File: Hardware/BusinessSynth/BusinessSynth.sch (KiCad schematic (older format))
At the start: 63 parts, among them J1 StylusKey, J2 StylusKey, J3 StylusKey, J4 StylusKey, J5 StylusKey, J6 StylusKey, J7 StylusKey, J8 StylusKey, J9 StylusKey, Q1 Q_PNP_BEC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

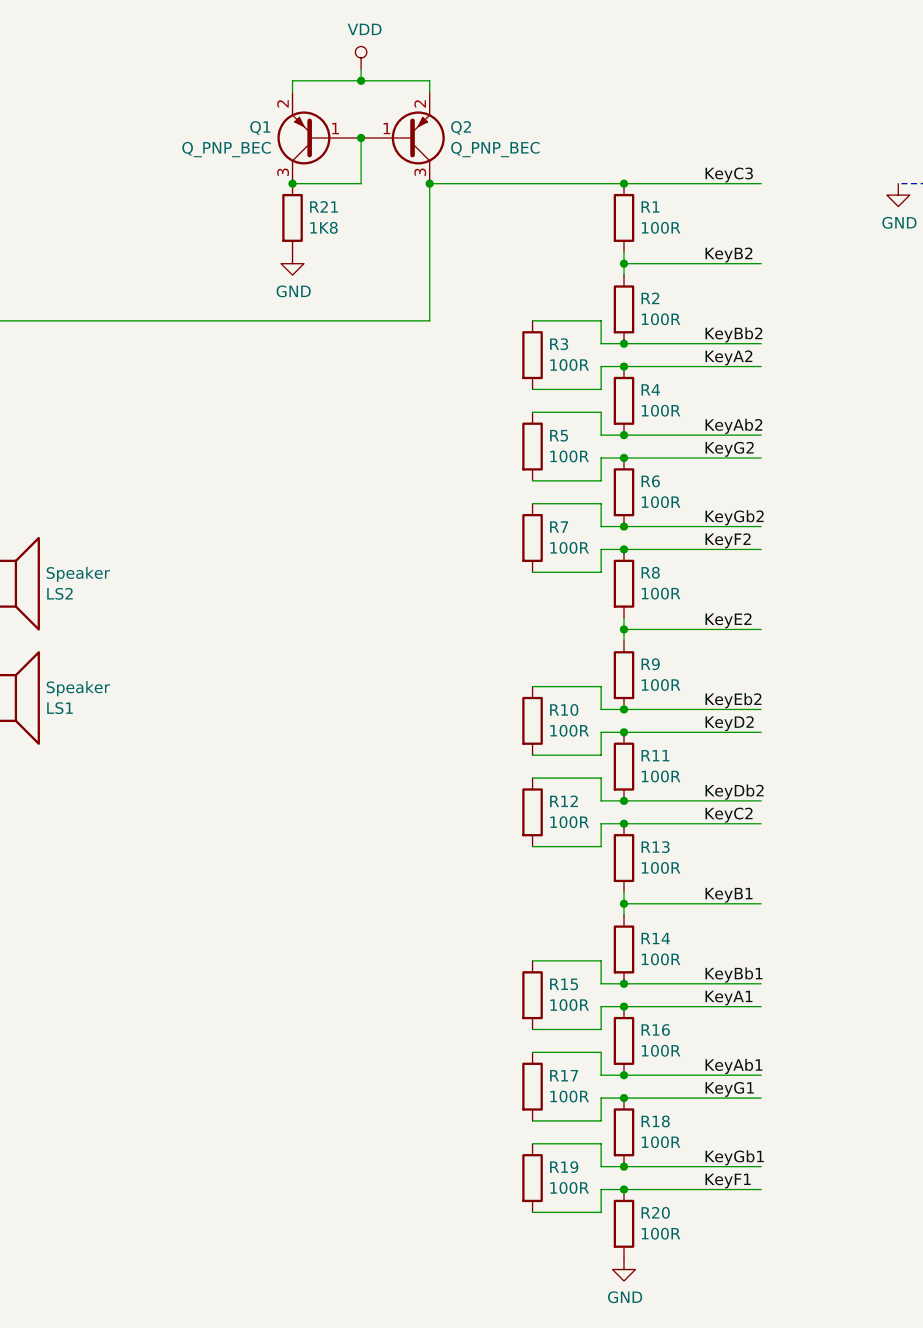
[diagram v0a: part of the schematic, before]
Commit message: Draw new keyboard circuit in the KiCAD schematic
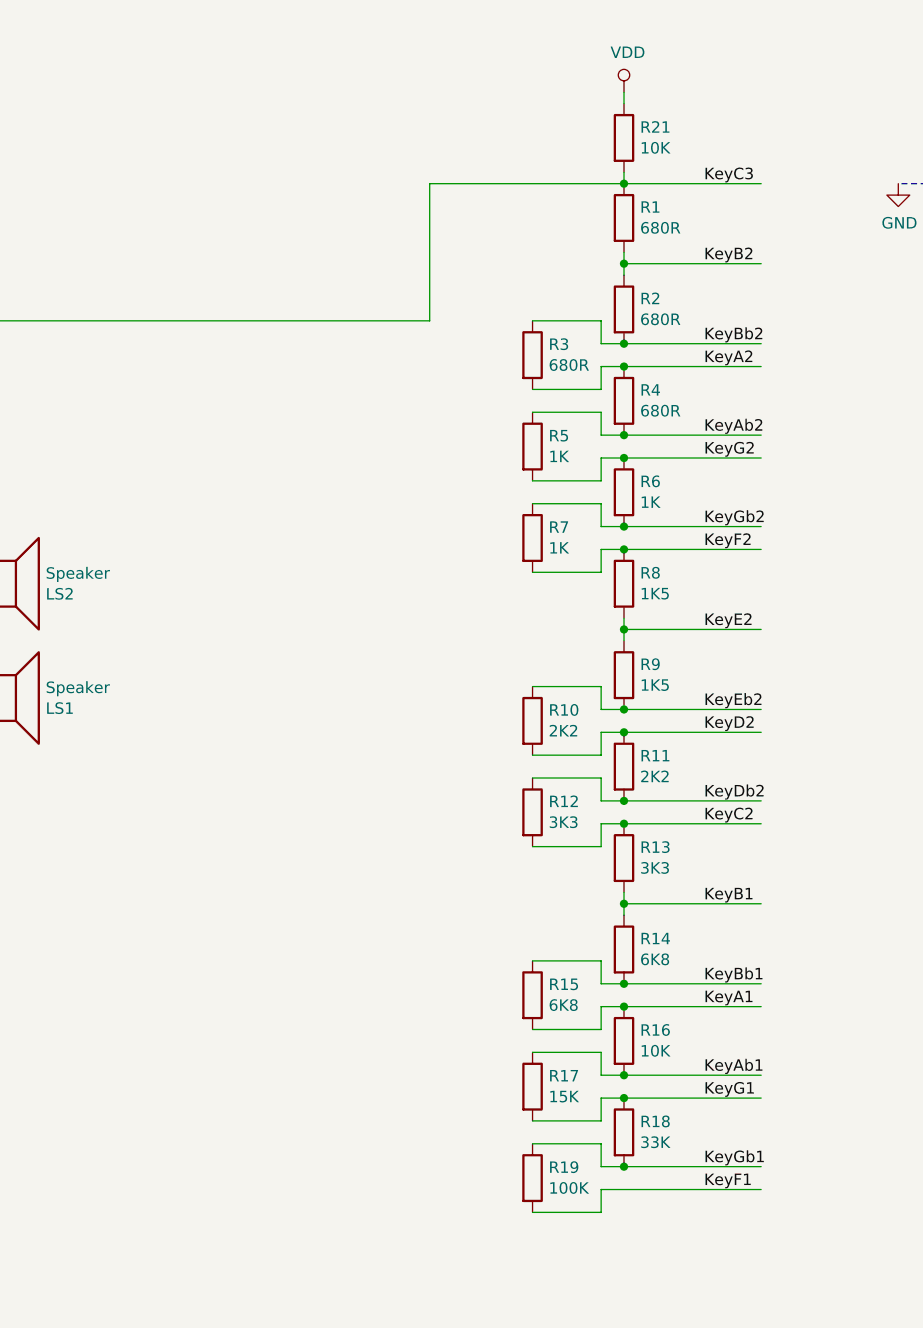
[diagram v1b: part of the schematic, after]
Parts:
- removed Q1, Q2: Q_PNP_BEC, BusinessSynth:SOT-323_SC-70_nosilk, symbol Device:Q_PNP_BEC
- removed R20: 100R, BusinessSynth:R_0603_1608Metric_nosilk, symbol Device:R
- R1, R2, R3, R4: value 100R -> 680R
- R10, R11: value 100R -> 2K2
- R12, R13: value 100R -> 3K3
- R14, R15: value 100R -> 6K8
- R16: value 100R -> 10K
- R17: value 100R -> 15K
- R18: value 100R -> 33K
- R19: value 100R -> 100K
- R21: value 1K8 -> 10K
- R5, R6, R7: value 100R -> 1K
- R8, R9: value 100R -> 1K5
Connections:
- wire segments 177 -> 171
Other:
- moved on the sheet: R21
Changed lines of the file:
@@
 P 9350 1450
 F 0 "R1" H 9420 1496 50  0000 L CNN
-F 1 "100R" H 9420 1405 50  0000 L CNN
+F 1 "680R" H 9420 1405 50  0000 L CNN
 F 2 "BusinessSynth:R_0603_1608Metric_nosilk" V 9280 1450 50  0001 C CNN
 F 3 "~" H 9350 1450 50  0001 C CNN
@@
 P 9350 1850
 F 0 "R2" H 9420 1896 50  0000 L CNN
-F 1 "100R" H 9420 1805 50  0000 L CNN
+F 1 "680R" H 9420 1805 50  0000 L CNN
 F 2 "BusinessSynth:R_0603_1608Metric_nosilk" V 9280 1850 50  0001 C CNN
 F 3 "~" H 9350 1850 50  0001 C CNN
@@
 P 9350 2250
 F 0 "R4" H 9420 2296 50  0000 L CNN
-F 1 "100R" H 9420 2205 50  0000 L CNN
+F 1 "680R" H 9420 2205 50  0000 L CNN
 F 2 "BusinessSynth:R_0603_1608Metric_nosilk" V 9280 2250 50  0001 C CNN
 F 3 "~" H 9350 2250 50  0001 C CNN
@@
 P 9350 2650
 F 0 "R6" H 9420 2696 50  0000 L CNN
-F 1 "100R" H 9420 2605 50  0000 L CNN
+F 1 "1K" H 9420 2605 50  0000 L CNN
 F 2 "BusinessSynth:R_0603_1608Metric_nosilk" V 9280 2650 50  0001 C CNN
 F 3 "~" H 9350 2650 50  0001 C CNN
@@
 P 9350 3050
 F 0 "R8" H 9420 3096 50  0000 L CNN
-F 1 "100R" H 9420 3005 50  0000 L CNN
+F 1 "1K5" H 9420 3005 50  0000 L CNN
 F 2 "BusinessSynth:R_0603_1608Metric_nosilk" V 9280 3050 50  0001 C CNN
 F 3 "~" H 9350 3050 50  0001 C CNN
@@
 P 9350 3450
 F 0 "R9" H 9420 3496 50  0000 L CNN
-F 1 "100R" H 9420 3405 50  0000 L CNN
+F 1 "1K5" H 9420 3405 50  0000 L CNN
 F 2 "BusinessSynth:R_0603_1608Metric_nosilk" V 9280 3450 50  0001 C CNN
 F 3 "~" H 9350 3450 50  0001 C CNN
@@
 P 9350 3850
 F 0 "R11" H 9420 3896 50  0000 L CNN
-F 1 "100R" H 9420 3805 50  0000 L CNN
+F 1 "2K2" H 9420 3805 50  0000 L CNN
 F 2 "BusinessSynth:R_0603_1608Metric_nosilk" V 9280 3850 50  0001 C CNN
 F 3 "~" H 9350 3850 50  0001 C CNN
@@
 P 9350 4250
 F 0 "R13" H 9420 4296 50  0000 L CNN
-F 1 "100R" H 9420 4205 50  0000 L CNN
+F 1 "3K3" H 9420 4205 50  0000 L CNN
 F 2 "BusinessSynth:R_0603_1608Metric_nosilk" V 9280 4250 50  0001 C CNN
 F 3 "~" H 9350 4250 50  0001 C CNN
@@
 P 9350 4650
 F 0 "R14" H 9420 4696 50  0000 L CNN
-F 1 "100R" H 9420 4605 50  0000 L CNN
+F 1 "6K8" H 9420 4605 50  0000 L CNN
 F 2 "BusinessSynth:R_0603_1608Metric_nosilk" V 9280 4650 50  0001 C CNN
 F 3 "~" H 9350 4650 50  0001 C CNN
@@
 P 9350 5050
 F 0 "R16" H 9420 5096 50  0000 L CNN
-F 1 "100R" H 9420 5005 50  0000 L CNN
+F 1 "10K" H 9420 5005 50  0000 L CNN
 F 2 "BusinessSynth:R_0603_1608Metric_nosilk" V 9280 5050 50  0001 C CNN
 F 3 "~" H 9350 5050 50  0001 C CNN
@@
 P 9350 5450
 F 0 "R18" H 9420 5496 50  0000 L CNN
-F 1 "100R" H 9420 5405 50  0000 L CNN
+F 1 "33K" H 9420 5405 50  0000 L CNN
 F 2 "BusinessSynth:R_0603_1608Metric_nosilk" V 9280 5450 50  0001 C CNN
 F 3 "~" H 9350 5450 50  0001 C CNN
 	1    9350 5450
-	1    0    0    -1
-$EndComp
-$Comp
-L Device:R R20
-U 1 1 5CA2AC61
-P 9350 5850
-F 0 "R20" H 9420 5896 50  0000 L CNN
-F 1 "100R" H 9420 5805 50  0000 L CNN
-F 2 "BusinessSynth:R_0603_1608Metric_nosilk" V 9280 5850 50  0001 C CNN
-F 3 "~" H 9350 5850 50  0001 C CNN
-	1    9350 5850
 	1    0    0    -1
 $EndComp
@@
 P 8950 2050
 F 0 "R3" H 9020 2096 50  0000 L CNN
-F 1 "100R" H 9020 2005 50  0000 L CNN
+F 1 "680R" H 9020 2005 50  0000 L CNN
 F 2 "BusinessSynth:R_0603_1608Metric_nosilk" V 8880 2050 50  0001 C CNN
 F 3 "~" H 8950 2050 50  0001 C CNN
@@
 P 8950 2450
 F 0 "R5" H 9020 2496 50  0000 L CNN
-F 1 "100R" H 9020 2405 50  0000 L CNN
+F 1 "1K" H 9020 2405 50  0000 L CNN
 F 2 "BusinessSynth:R_0603_1608Metric_nosilk" V 8880 2450 50  0001 C CNN
 F 3 "~" H 8950 2450 50  0001 C CNN
@@
 P 8950 2850
 F 0 "R7" H 9020 2896 50  0000 L CNN
-F 1 "100R" H 9020 2805 50  0000 L CNN
+F 1 "1K" H 9020 2805 50  0000 L CNN
 F 2 "BusinessSynth:R_0603_1608Metric_nosilk" V 8880 2850 50  0001 C CNN
 F 3 "~" H 8950 2850 50  0001 C CNN
@@
 P 8950 3650
 F 0 "R10" H 9020 3696 50  0000 L CNN
-F 1 "100R" H 9020 3605 50  0000 L CNN
+F 1 "2K2" H 9020 3605 50  0000 L CNN
 F 2 "BusinessSynth:R_0603_1608Metric_nosilk" V 8880 3650 50  0001 C CNN
 F 3 "~" H 8950 3650 50  0001 C CNN
@@
 P 8950 4050
 F 0 "R12" H 9020 4096 50  0000 L CNN
-F 1 "100R" H 9020 4005 50  0000 L CNN
+F 1 "3K3" H 9020 4005 50  0000 L CNN
 F 2 "BusinessSynth:R_0603_1608Metric_nosilk" V 8880 4050 50  0001 C CNN
 F 3 "~" H 8950 4050 50  0001 C CNN
@@
 P 8950 4850
 F 0 "R15" H 9020 4896 50  0000 L CNN
-F 1 "100R" H 9020 4805 50  0000 L CNN
+F 1 "6K8" H 9020 4805 50  0000 L CNN
 F 2 "BusinessSynth:R_0603_1608Metric_nosilk" V 8880 4850 50  0001 C CNN
 F 3 "~" H 8950 4850 50  0001 C CNN
@@
 P 8950 5250
 F 0 "R17" H 9020 5296 50  0000 L CNN
-F 1 "100R" H 9020 5205 50  0000 L CNN
+F 1 "15K" H 9020 5205 50  0000 L CNN
 F 2 "BusinessSynth:R_0603_1608Metric_nosilk" V 8880 5250 50  0001 C CNN
 F 3 "~" H 8950 5250 50  0001 C CNN
@@
 P 8950 5650
 F 0 "R19" H 9020 5696 50  0000 L CNN
-F 1 "100R" H 9020 5605 50  0000 L CNN
+F 1 "100K" H 9020 5605 50  0000 L CNN
 F 2 "BusinessSynth:R_0603_1608Metric_nosilk" V 8880 5650 50  0001 C CNN
 F 3 "~" H 8950 5650 50  0001 C CNN
@@
 	9250 5800 9250 5700
 Wire Wire Line
-	9250 5700 9350 5700
-Wire Wire Line
-	9350 5700 9950 5700
-Connection ~ 9350 5700
-Wire Wire Line
 	9350 5600 9950 5600
 Connection ~ 9350 5600
@@
 Wire Wire Line
 	9350 1300 9950 1300
-$Comp
-L power:GND #PWR06
-U 1 1 5CA52483
-P 9350 6000
-F 0 "#PWR06" H 9350 5750 50  0001 C CNN
-F 1 "GND" H 9355 5827 50  0000 C CNN
-F 2 "" H 9350 6000 50  0001 C CNN
-F 3 "" H 9350 6000 50  0001 C CNN
-	1    9350 6000
-	1    0    0    -1
-$EndComp
 Text Label 9700 1300 0    50   ~ 0
 KeyC3
@@
 L Device:R R21
 U 1 1 5CA2F499
-P 7900 1450
-F 0 "R21" H 7970 1496 50  0000 L CNN
-F 1 "1K8" H 7970 1405 50  0000 L CNN
-F 2 "Resistor_SMD:R_0402_1005Metric" V 7830 1450 50  0001 C CNN
-F 3 "~" H 7900 1450 50  0001 C CNN
-	1    7900 1450
-	1    0    0    -1
-$EndComp
-$Comp
-L power:GND #PWR0104
-U 1 1 5CA2FA03
-P 7900 1600
-F 0 "#PWR0104" H 7900 1350 50  0001 C CNN
-F 1 "GND" H 7905 1427 50  0000 C CNN
-F 2 "" H 7900 1600 50  0001 C CNN
-F 3 "" H 7900 1600 50  0001 C CNN
-	1    7900 1600
+P 9350 1100
+F 0 "R21" H 9420 1146 50  0000 L CNN
+F 1 "10K" H 9420 1055 50  0000 L CNN
+F 2 "Resistor_SMD:R_0402_1005Metric" V 9280 1100 50  0001 C CNN
+F 3 "~" H 9350 1100 50  0001 C CNN
+	1    9350 1100
 	1    0    0    -1
 $EndComp
@@
 L power:VDD #PWR0105
 U 1 1 5CA35224
-P 8200 800
-F 0 "#PWR0105" H 8200 650 50  0001 C CNN
-F 1 "VDD" H 8217 973 50  0000 C CNN
-F 2 "" H 8200 800 50  0001 C CNN
-F 3 "" H 8200 800 50  0001 C CNN
-	1    8200 800
-	1    0    0    -1
-$EndComp
-Wire Wire Line
-	7900 850  7900 900
-Wire Wire Line
-	7900 850  8200 850
-Wire Wire Line
-	8200 850  8200 800
-Connection ~ 8200 850
-Wire Wire Line
-	8200 850  8500 850
-Wire Wire Line
-	8200 1100 8200 1300
-Wire Wire Line
-	8200 1300 7900 1300
+P 9350 900
+F 0 "#PWR0105" H 9350 750 50  0001 C CNN
+F 1 "VDD" H 9367 1073 50  0000 C CNN
+F 2 "" H 9350 900 50  0001 C CNN
+F 3 "" H 9350 900 50  0001 C CNN
+	1    9350 900
+	1    0    0    -1
+$EndComp
+Wire Wire Line
+	9350 950  9350 900
 Wire Wire Line
 	9350 1300 8500 1300
@@
 Text Label 3350 2650 2    50   ~ 0
 KeyboardVoltage
-Wire Wire Line
-	8500 850  8500 900
 Wire Wire Line
 	8500 1900 4000 1900
@@
 	1    0    0    -1
 $EndComp
-$Comp
-L Device:Q_PNP_BEC Q2
-U 1 1 5CE2D45B
-P 8400 1100
-F 0 "Q2" H 8590 1054 50  0000 L CNN
-F 1 "Q_PNP_BEC" H 8590 1145 50  0000 L CNN
-F 2 "BusinessSynth:SOT-323_SC-70_nosilk" H 8600 1200 50  0001 C CNN
-F 3 "~" H 8400 1100 50  0001 C CNN
-	1    8400 1100
-	1    0    0    1
-$EndComp
-$Comp
-L Device:Q_PNP_BEC Q1
-U 1 1 5CE2E126
-P 8000 1100
-F 0 "Q1" H 8191 1054 50  0000 L CNN
-F 1 "Q_PNP_BEC" H 8191 1145 50  0000 L CNN
-F 2 "BusinessSynth:SOT-323_SC-70_nosilk" H 8200 1200 50  0001 C CNN
-F 3 "~" H 8000 1100 50  0001 C CNN
-	1    8000 1100
-	-1   0    0    1
-$EndComp
-Connection ~ 7900 1300
-Connection ~ 8200 1100
-Connection ~ 8500 1300
+Wire Wire Line
+	9250 5700 9950 5700
+Wire Wire Line
+	9350 1250 9350 1300
 $EndSCHEMATC

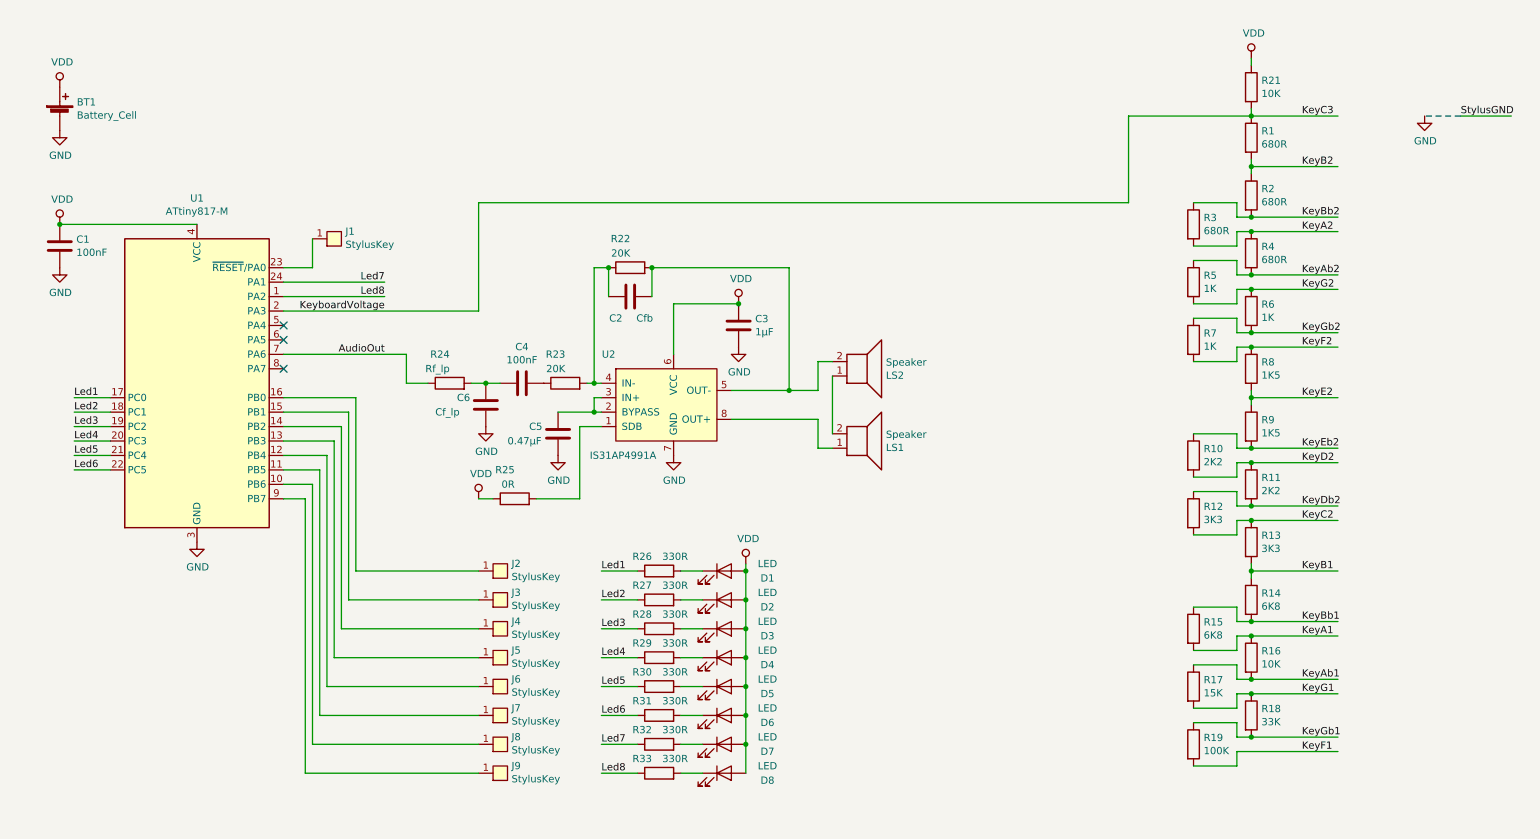
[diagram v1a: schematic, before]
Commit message: Change resistor chain in schematic to simpler solution
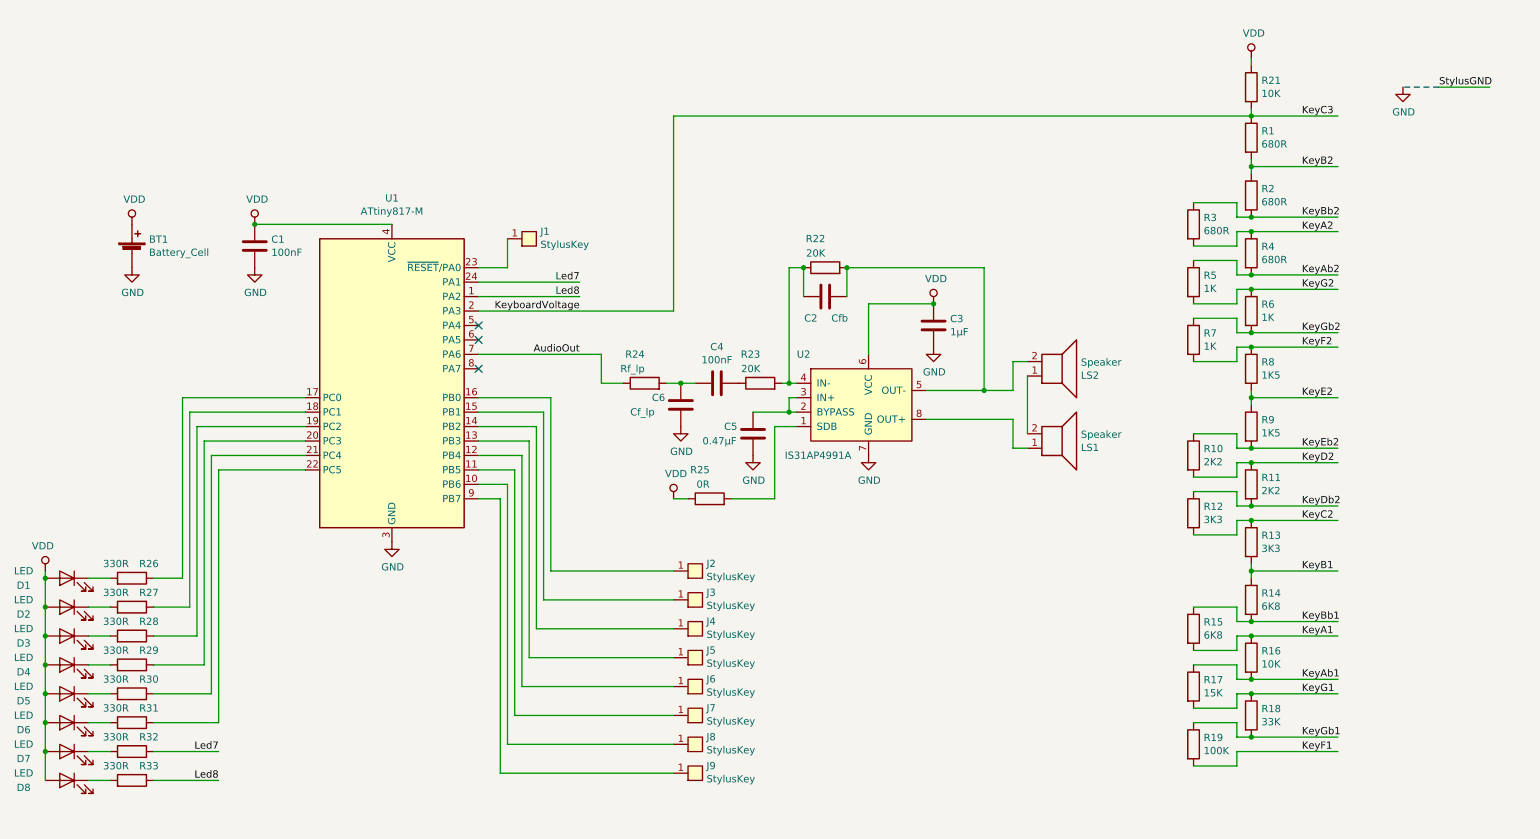
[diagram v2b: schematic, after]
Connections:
- net labels removed: Led1, Led2, Led3, Led4, Led5, Led6
- wire segments 171 -> 175
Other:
- moved on the sheet: BT1, C1, C2, C3, C4, C5, C6, D1, D2, D3, D4, D5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

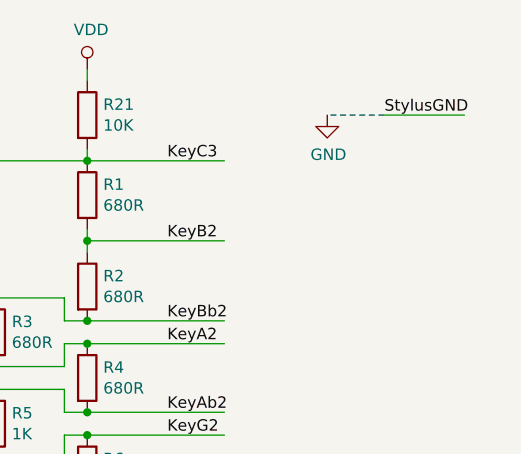
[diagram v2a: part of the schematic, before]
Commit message: Fix speaker-driver footprint, and complete new routing
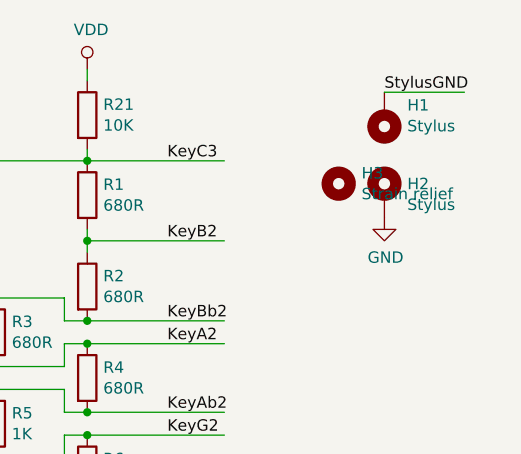
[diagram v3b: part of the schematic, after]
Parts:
- added H1, H2: Stylus, Connector_Wire:SolderWirePad_1x01_Drill0.8mm, symbol Mechanical:MountingHole_Pad
- added H3: Strain relief, MountingHole:MountingHole_2.1mm, symbol Mechanical:MountingHole
- U2: footprint BusinessSynth:SOP-8_3.76x4.96mm_P1.27mm_nosilk -> BusinessSynth:MSOP-8-1EP_3x3mm_P0.65mm_nosilk
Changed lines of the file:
@@
 Text Label 9700 5700 0    50   ~ 0
 KeyF1
-Text Label 10650 1100 0    50   ~ 0
+Text Label 10650 1000 0    50   ~ 0
 StylusGND
 Wire Wire Line
-	11000 1100 10650 1100
+	11000 1000 10650 1000
 $Comp
 L power:GND #PWR0103
 U 1 1 5CAD8391
-P 10400 1100
-F 0 "#PWR0103" H 10400 850 50  0001 C CNN
-F 1 "GND" H 10405 927 50  0000 C CNN
-F 2 "" H 10400 1100 50  0001 C CNN
-F 3 "" H 10400 1100 50  0001 C CNN
-	1    10400 1100
-	1    0    0    -1
-$EndComp
-Wire Notes Line
-	10650 1100 10400 1100
+P 10650 1550
+F 0 "#PWR0103" H 10650 1300 50  0001 C CNN
+F 1 "GND" H 10655 1377 50  0000 C CNN
+F 2 "" H 10650 1550 50  0001 C CNN
+F 3 "" H 10650 1550 50  0001 C CNN
+	1    10650 1550
+	1    0    0    -1
+$EndComp
 $Comp
 L Device:R R21
@@
 F 0 "U2" H 6250 3650 50  0000 C CNN
 F 1 "IS31AP4991A" H 6350 2950 50  0000 C CNN
-F 2 "BusinessSynth:SOP-8_3.76x4.96mm_P1.27mm_nosilk" H 6650 3700 50  0001 C CNN
+F 2 "BusinessSynth:MSOP-8-1EP_3x3mm_P0.65mm_nosilk" H 6650 3700 50  0001 C CNN
 F 3 "" H 6650 3700 50  0001 C CNN
 	1    6650 3300
@@
 	1    0    0    -1
 $EndComp
+$Comp
+L Mechanical:MountingHole_Pad H2
+U 1 1 5D641935
+P 10650 1450
+F 0 "H2" H 10750 1499 50  0000 L CNN
+F 1 "Stylus" H 10750 1408 50  0000 L CNN
+F 2 "Connector_Wire:SolderWirePad_1x01_Drill0.8mm" H 10650 1450 50  0001 C CNN
+F 3 "~" H 10650 1450 50  0001 C CNN
+	1    10650 1450
+	1    0    0    -1
+$EndComp
+$Comp
+L Mechanical:MountingHole_Pad H1
+U 1 1 5D663F95
+P 10650 1100
+F 0 "H1" H 10550 1057 50  0000 R CNN
+F 1 "Stylus" H 10550 1148 50  0000 R CNN
+F 2 "Connector_Wire:SolderWirePad_1x01_Drill0.8mm" H 10650 1100 50  0001 C CNN
+F 3 "~" H 10650 1100 50  0001 C CNN
+	1    10650 1100
+	-1   0    0    1
+$EndComp
+$Comp
+L Mechanical:MountingHole H3
+U 1 1 5D67C8D8
+P 10450 1400
+F 0 "H3" H 10550 1446 50  0000 L CNN
+F 1 "Strain relief" H 10550 1355 50  0000 L CNN
+F 2 "MountingHole:MountingHole_2.1mm" H 10450 1400 50  0001 C CNN
+F 3 "~" H 10450 1400 50  0001 C CNN
+	1    10450 1400
+	1    0    0    -1
+$EndComp
